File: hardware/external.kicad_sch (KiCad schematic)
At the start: 3 parts, among them J1 BASYS3, U1 MCP4728

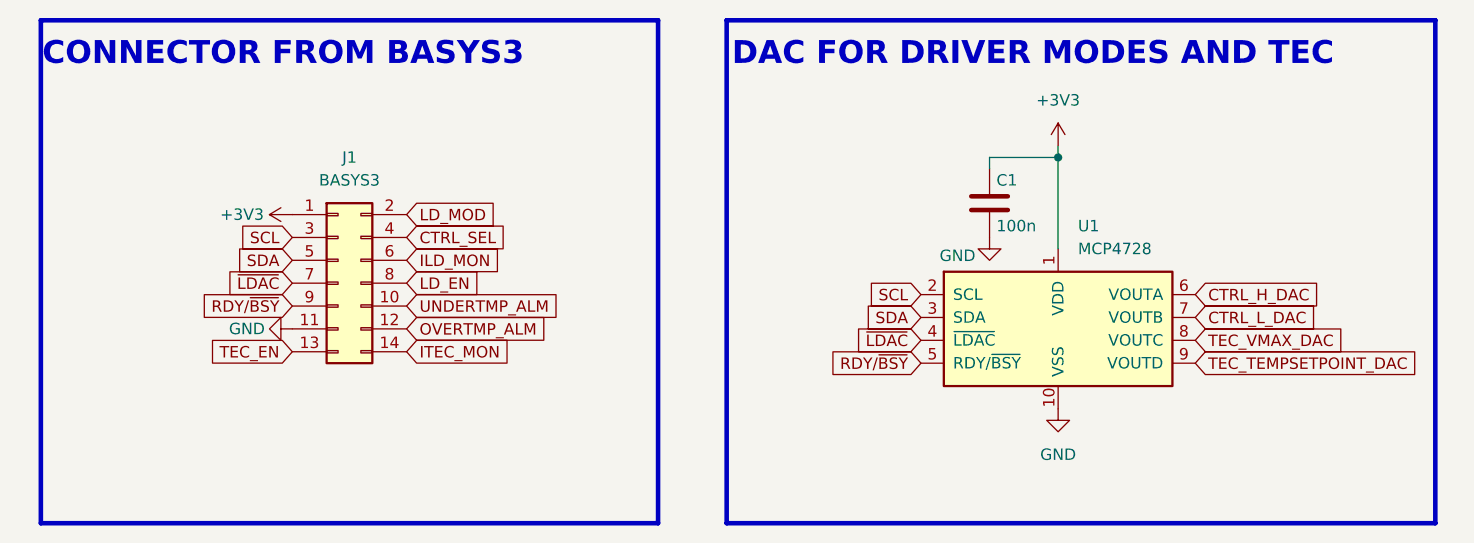
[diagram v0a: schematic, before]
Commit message: feat: UART communication working, now with transmitter to verify that the sent packet is correct
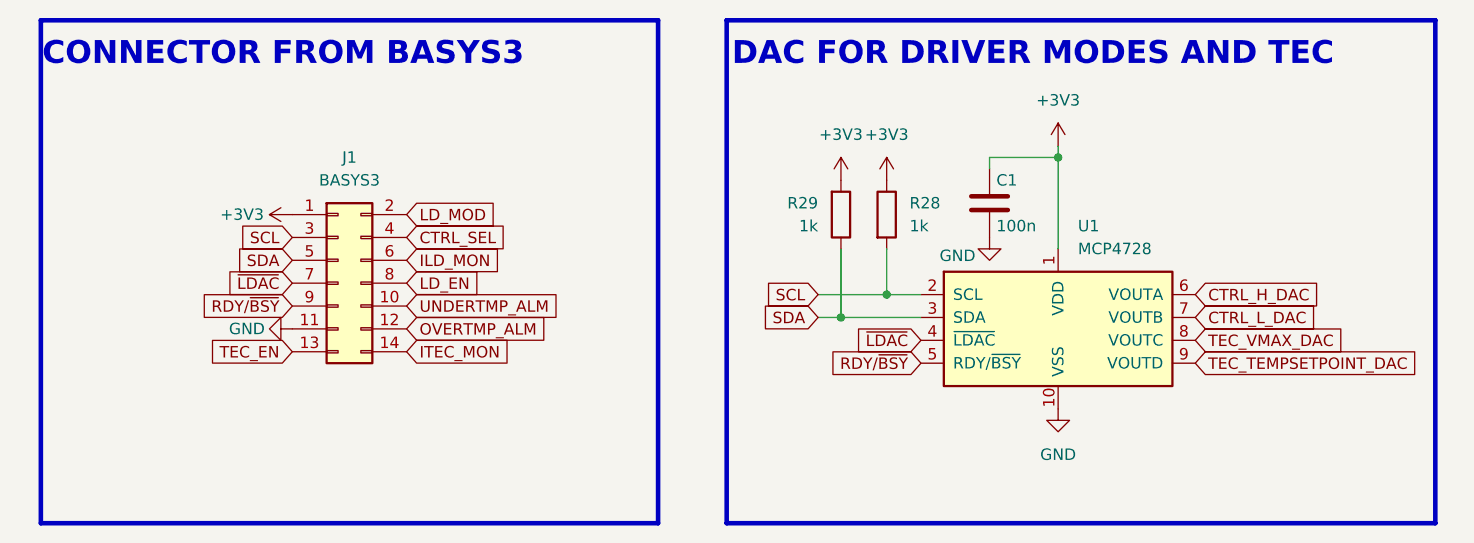
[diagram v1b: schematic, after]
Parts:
- added R28, R29: 1k, symbol Device:R
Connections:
- net +3V3: now also R28.1, R29.2
- net SCL: now also R28.2
- net SDA: now also R29.1

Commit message: feat: decent readme as user manual
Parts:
- removed R28, R29: 1k, symbol Device:R
- added R28: 10, Resistor_SMD:R_0603_1608Metric, symbol Device:R_Small
- added R29: 1k, Resistor_SMD:R_0603_1608Metric, symbol Device:R_Small
- J1: footprint Connector_PinHeader_2.54mm:PinHeader_2x07_P2.54mm_Horizontal -> Connector_PinHeader_2.54mm:PinHeader_2x07_P2.54mm_Vertical
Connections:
- net +3V3: now also R28.2, R29.2
- net SCL: now also R28.1
- net SDA: now also R29.1
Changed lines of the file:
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@@
 	(wire
 		(pts
-			(xy 160.02 93.98) (xy 160.02 101.6)
+			(xy 176.53 83.82) (xy 176.53 85.09)
 		)
 		(stroke
@@
 	(wire
 		(pts
-			(xy 176.53 83.82) (xy 176.53 85.09)
+			(xy 160.02 86.36) (xy 160.02 87.63)
 		)
 		(stroke
@@
 	(wire
 		(pts
-			(xy 165.1 93.98) (xy 165.1 99.06)
+			(xy 165.1 86.36) (xy 165.1 87.63)
 		)
 		(stroke
@@
 		)
 	)
+	(wire
+		(pts
+			(xy 165.1 92.71) (xy 165.1 99.06)
+		)
+		(stroke
+			(width 0)
+			(type default)
+		)
+	)
 	(polyline
 		(pts
@@
 		(pts
 			(xy 184.15 83.82) (xy 184.15 93.98)
+		)
+		(stroke
+			(width 0)
+			(type default)
+		)
+	)
+	(wire
+		(pts
+			(xy 160.02 92.71) (xy 160.02 101.6)
 		)
 		(stroke
@@
 	)
 	(symbol
-		(lib_id "Device:R")
-		(at 165.1 90.17 0)
+		(lib_id "Device:R_Small")
+		(at 165.1 90.17 180)
 		(unit 1)
 		(exclude_from_sim no)
@@
 		(on_board yes)
 		(dnp no)
-		(fields_autoplaced yes)
 		(property "Reference" "R28"
-			(at 167.64 88.8999 0)
-			(effects
-				(font
-					(size 1.27 1.27)
-				)
-				(justify left)
-			)
-		)
-		(property "Value" "1k"
-			(at 167.64 91.4399 0)
-			(effects
-				(font
-					(size 1.27 1.27)
-				)
-				(justify left)
-			)
-		)
-		(property "Footprint" ""
-			(at 163.322 90.17 90)
+			(at 170.688 88.646 0)
+			(effects
+				(font
+					(size 1.27 1.27)
+				)
+				(justify left)
+			)
+		)
+		(property "Value" "10"
+			(at 169.672 90.424 0)
+			(effects
+				(font
+					(size 1.27 1.27)
+				)
+				(justify left)
+			)
+		)
+		(property "Footprint" "Resistor_SMD:R_0603_1608Metric"
+			(at 165.1 90.17 0)
 			(effects
 				(font
@@
 			)
 		)
-		(property "Description" "Resistor"
+		(property "Description" "Resistor, small symbol"
 			(at 165.1 90.17 0)
 			(effects
@@
 			)
 		)
+		(property "Sim.Device" ""
+			(at 165.1 90.17 0)
+			(effects
+				(font
+					(size 1.27 1.27)
+				)
+				(hide yes)
+			)
+		)
+		(property "Sim.Pins" ""
+			(at 165.1 90.17 0)
+			(effects
+				(font
+					(size 1.27 1.27)
+				)
+				(hide yes)
+			)
+		)
+		(property "Sim.Type" ""
+			(at 165.1 90.17 0)
+			(effects
+				(font
+					(size 1.27 1.27)
+				)
+				(hide yes)
+			)
+		)
+		(property "PN" "CRCW060310R0FKEAC "
+			(at 165.1 90.17 0)
+			(effects
+				(font
+					(size 1.27 1.27)
+				)
+				(hide yes)
+			)
+		)
+		(property "Store Link" "https://www.mouser.it/ProductDetail/Vishay-Dale/CRCW060310R0FKEAC?qs=E3Y5ESvWgWP5XvJ40P8QAg%3D%3D"
+			(at 165.1 90.17 0)
+			(effects
+				(font
+					(size 1.27 1.27)
+				)
+				(hide yes)
+			)
+		)
 		(pin "2"
 		)
@@
 		)
 		(instances
-			(project ""
+			(project "SOA-driver"
 				(path "/aef12ca3-3d60-44eb-99b6-8bdd18a4b35c/b8096563-2aa1-42a7-b303-2d7d794c80ce"
 					(reference "R28")
@@
 	)
 	(symbol
-		(lib_id "Device:R")
+		(lib_id "Device:R_Small")
 		(at 160.02 90.17 0)
 		(mirror x)
@@
 		(on_board yes)
 		(dnp no)
-		(fields_autoplaced yes)
 		(property "Reference" "R29"
-			(at 157.48 88.8999 0)
-			(effects
-				(font
-					(size 1.27 1.27)
-				)
-				(justify right)
+			(at 154.432 88.646 0)
+			(effects
+				(font
+					(size 1.27 1.27)
+				)
+				(justify left)
 			)
 		)
 		(property "Value" "1k"
-			(at 157.48 91.4399 0)
-			(effects
-				(font
-					(size 1.27 1.27)
-				)
-				(justify right)
-			)
-		)
-		(property "Footprint" ""
-			(at 158.242 90.17 90)
+			(at 155.448 90.424 0)
+			(effects
+				(font
+					(size 1.27 1.27)
+				)
+				(justify left)
+			)
+		)
+		(property "Footprint" "Resistor_SMD:R_0603_1608Metric"
+			(at 160.02 90.17 0)
 			(effects
 				(font
@@
 			)
 		)
-		(property "Description" "Resistor"
+		(property "Description" "Resistor, small symbol"
 			(at 160.02 90.17 0)
 			(effects
@@
 			)
 		)
+		(property "Sim.Device" ""
+			(at 160.02 90.17 0)
+			(effects
+				(font
+					(size 1.27 1.27)
+				)
+				(hide yes)
+			)
+		)
+		(property "Sim.Pins" ""
+			(at 160.02 90.17 0)
+			(effects
+				(font
+					(size 1.27 1.27)
+				)
+				(hide yes)
+			)
+		)
+		(property "Sim.Type" ""
+			(at 160.02 90.17 0)
+			(effects
+				(font
+					(size 1.27 1.27)
+				)
+				(hide yes)
+			)
+		)
+		(property "PN" "CRCW060310R0FKEAC "
+			(at 160.02 90.17 0)
+			(effects
+				(font
+					(size 1.27 1.27)
+				)
+				(hide yes)
+			)
+		)
+		(property "Store Link" "https://www.mouser.it/ProductDetail/Vishay-Dale/CRCW060310R0FKEAC?qs=E3Y5ESvWgWP5XvJ40P8QAg%3D%3D"
+			(at 160.02 90.17 0)
+			(effects
+				(font
+					(size 1.27 1.27)
+				)
+				(hide yes)
+			)
+		)
 		(pin "2"
 		)
@@
 		)
 		(instances
-			(project ""
+			(project "SOA-driver"
 				(path "/aef12ca3-3d60-44eb-99b6-8bdd18a4b35c/b8096563-2aa1-42a7-b303-2d7d794c80ce"
 					(reference "R29")
@@
 			)
 		)
-		(property "Footprint" "Connector_PinHeader_2.54mm:PinHeader_2x07_P2.54mm_Horizontal"
+		(property "Footprint" "Connector_PinHeader_2.54mm:PinHeader_2x07_P2.54mm_Vertical"
 			(at 104.14 97.79 0)
 			(effects

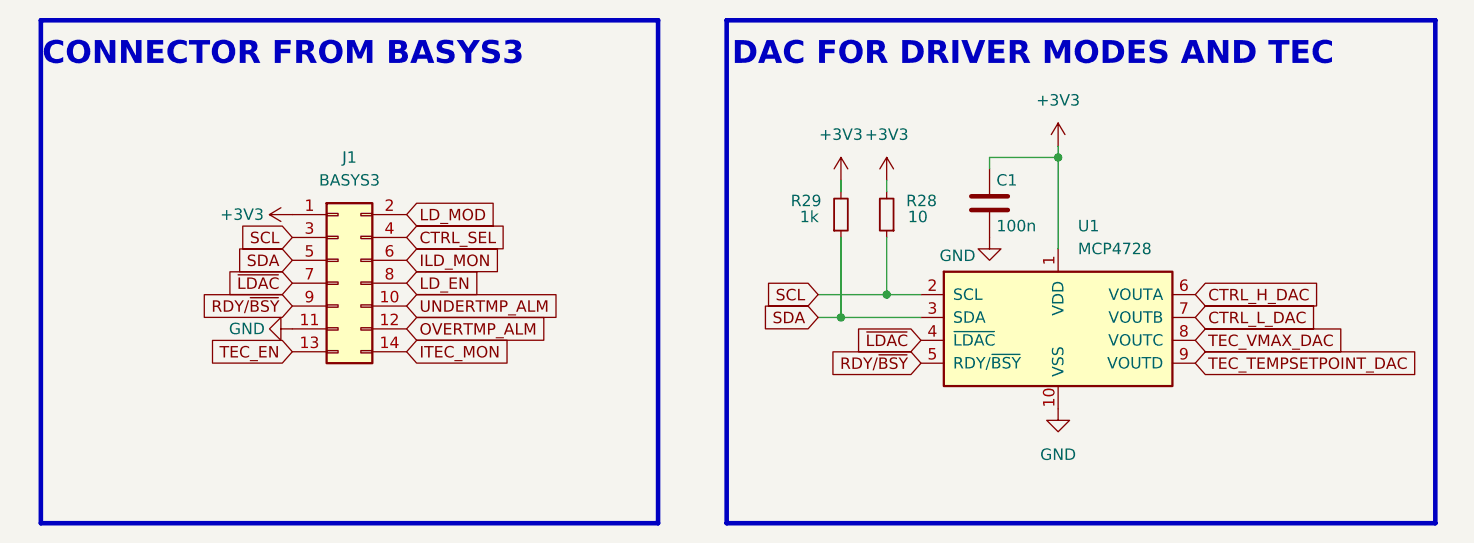
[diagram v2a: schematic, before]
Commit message: fix: I2C fixed and tested, modulation working with double threshold. feat: TEC and SOA can be enabled separately
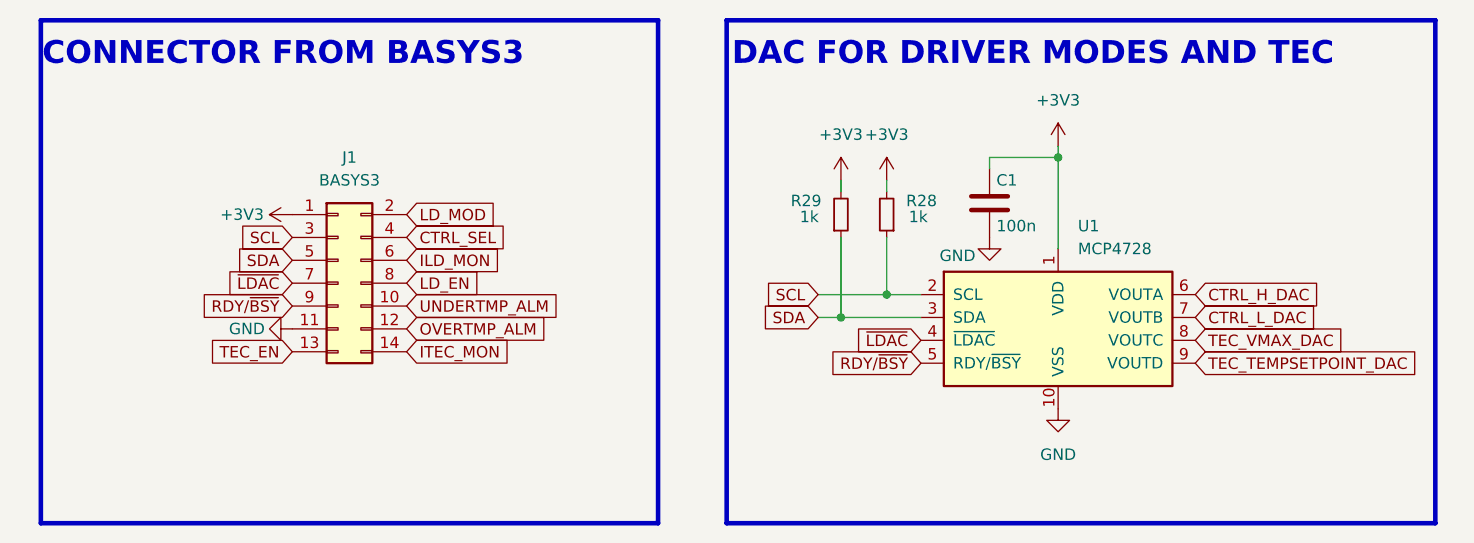
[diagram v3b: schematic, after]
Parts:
- R28: value 10 -> 1k
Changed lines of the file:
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@@
 			)
 		)
-		(property "Value" "10"
+		(property "Value" "1k"
 			(at 169.672 90.424 0)
 			(effects

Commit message: feat: syntethizing parser with output registers instead on using external reg, minor fixes to schematic and PCB
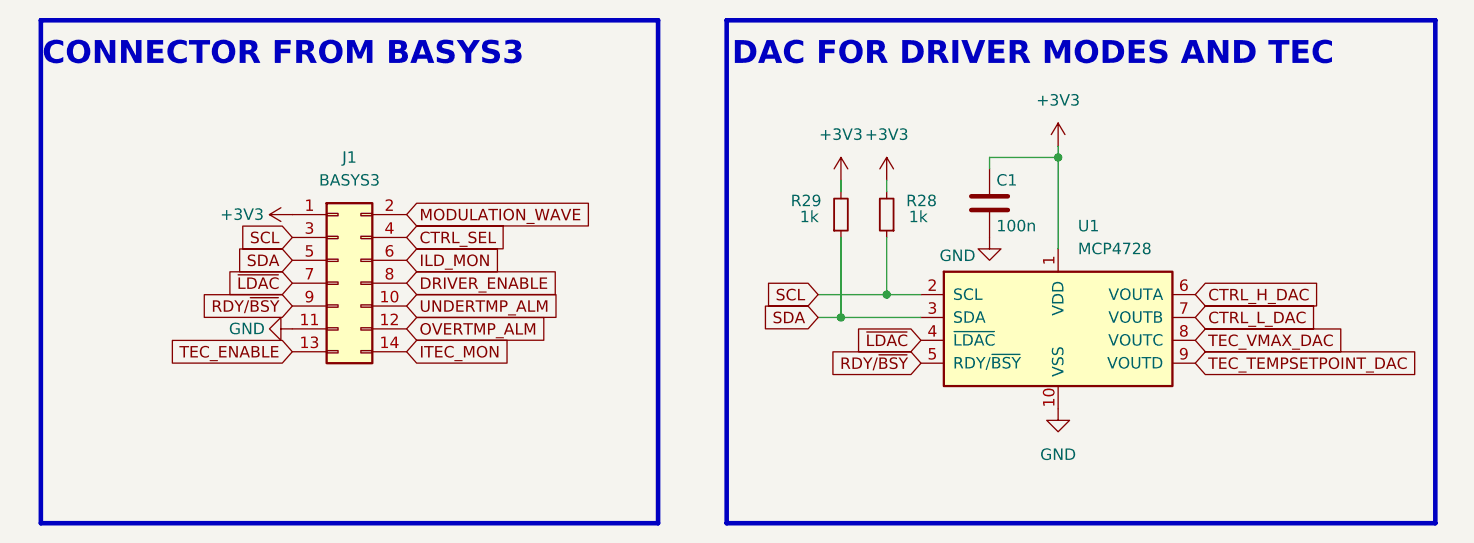
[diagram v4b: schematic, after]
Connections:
- net LD_EN renamed DRIVER_ENABLE
- net LD_MOD renamed MODULATION_WAVE
- net TEC_EN renamed TEC_ENABLE
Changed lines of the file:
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@@
 		)
 	)
-	(global_label "LD_MOD"
+	(global_label "MODULATION_WAVE"
 		(shape input)
 		(at 111.76 90.17 0)
@@
 		)
 		(property "Intersheetrefs" "${INTERSHEET_REFS}"
-			(at 122.0628 90.17 0)
+			(at 132.2229 90.17 0)
 			(effects
 				(font
@@
 		)
 	)
-	(global_label "TEC_EN"
+	(global_label "TEC_ENABLE"
 		(shape input)
 		(at 99.06 105.41 180)
@@
 		)
 		(property "Intersheetrefs" "${INTERSHEET_REFS}"
-			(at 89.2411 105.41 0)
+			(at 84.7054 105.41 0)
 			(effects
 				(font
@@
 		)
 	)
-	(global_label "LD_EN"
+	(global_label "DRIVER_ENABLE"
 		(shape input)
 		(at 111.76 97.79 0)
@@
 		)
 		(property "Intersheetrefs" "${INTERSHEET_REFS}"
-			(at 120.4904 97.79 0)
-			(effects
-				(font
+			(at 129.3804 97.79 0)
+			(effects
+				(font
